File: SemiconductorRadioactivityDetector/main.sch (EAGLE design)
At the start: 41 parts, among them IC1 78L08Z, IC2 OPA2333D, IC3 OPA2333D, J1 22-05-7028-02, Q1 2N4093

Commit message: Third HW revision, paritialy done.
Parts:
- removed C10: 4p7, resistor:C-EUC0805
- removed C11: 10n, resistor:C-EUC0805
- removed C12: 10n, rcl:C-EUC0805
- removed C13: 100n, rcl:C-EUC0805
- removed C14, C15, C9: 100p, resistor:C-EUC0805
- removed C16: 100n, resistor:C-EUC0805
- removed IC3: OPA2333D, linear:OPA2333D
- removed J1: 22-05-7028-02, con-molex:22-05-7028-02
- removed PAD1, PAD2: (no value), wirepad:1,6/0,8
- removed Q1: 2N4093, transistor-fet:2N4093
- removed R11: 1k, rcl:R-EU_R0805
- removed R12, R13: 10k, rcl:R-EU_R0805
- removed TP1, TP2, TP5: PTR1TP12R, testpad:PTR1TP12R
- added D2, D3: BPW32, opto-trans-siemens:BPW32
- added SL1: (no value), con-amp-quick:M02
- added U1: TPS7A470, regulator-jqi:TPS7A470
- added X1: LTI-SASF54GT, con-coax:LTI-SASF54GT
- C1, C5: value 100n -> 330n
- C2: value 330n -> (none); device rcl:C-EUC0805 -> resistor:CPOL-EUT/3528-12R
- C3: value 100u/16V -> 100n; device rcl:CPOL-EU153CLV-0505 -> rcl:C-EUC0805
- C6: value 10n -> 100n; device resistor:C-EUC0805 -> rcl:C-EUC0805
- C7: value 10n -> 330n; device resistor:C-EUC0805 -> rcl:C-EUC0805
- C8: value 100n -> 330n; device rcl:C-EUC0805 -> rcl:C-EUC1206K
- D1: value BP104 -> BPW32; device opto-trans-siemens:BP104 -> opto-trans-siemens:BPW32
- IC1: value 78L08Z -> LF356D; device linear:78L08Z -> linear:LF356D
- IC2: value OPA2333D -> LF356D; device linear:OPA2333D -> linear:LF356D
- R1: value 10M -> 10k; device resistor:R-EU_0204/2V -> rcl:R-EU_R1206
- R10, R7: value 1k -> 10k
- R3: value 10k -> (none); device rcl:R-EU_R0805 -> resistor:R-EU_MELF0204W
- R4: value 470k -> (none); device rcl:R-EU_R0805 -> resistor:R-EU_MELF0204W
- R5: value 39k -> (none); device rcl:R-EU_R0805 -> resistor:R-TRIMM64W
- R6: value 10R -> (none); device rcl:R-EU_R0805 -> resistor:R-EU_M0805
- R8: value 10k -> (none); device rcl:R-EU_R0805 -> resistor:R-EU_M0805
- R9: value 10M -> (none); device rcl:R-EU_0204/2V -> resistor:R-EU_M0805
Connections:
- removed net N$11: C7.2, R7.2
- removed net N$13: C14.1, IC2B.-IN, R11.1, R12.2
- removed net N$16: C2.1, D1.C, R4.2
- removed net N$17: D1.A, Q1.G, R1.1
- removed net N$20: C10.2, C11.1, IC3A.OUT, R9.1
- removed net N$22: C12.1, C9.2, IC2A.OUT, R8.1
- removed net V_REF: C1.1, IC2A.+IN, IC2B.+IN, IC3A.+IN, IC3B.+IN, R2.1, R3.2, TP1.TP
- new net N$1: C5.2, C8.1, IC1.OUT, R4.2
- new net N$5: C6.1, U1.NR
- net GND: now also C2.-, C3.2, C6.2, C7.2, D1.A, D2.A, D3.A, IC1.V-, IC2.V-, R10.1, R2.1, R6.1, SL1.1, U1.0.1, U1.0.2, U1.0.4, U1.0.8, U1.1.6, U1.3.2, U1.6.4A, U1.6.4B, U1.GND, X1.2; no longer C13.2, C16.2, C2.2, C3.-, C5.2, C8.2, IC1.GND, IC2P.V-, IC3P.V-, J1-2.S, PAD2.P, Q1.S, R1.2, R3.1
- net N$10: now also C8.2, IC2.+IN, R10.2; no longer C9.1, IC2A.-IN, R8.2
- net N$14: now also C1.1, IC1.+IN, R1.1, R2.2; no longer C12.2, R11.2
- net N$15: now also R9.2, X1.1; no longer C11.2, R10.2
- net N$2: now also IC2.-IN, R8.1; no longer C6.2
- net N$3: now also R3.2, R4.1; no longer C14.2, IC2B.OUT, PAD1.P, R12.1
- net N$4: now also C5.1, D1.C, D2.C, D3.C, IC1.-IN, R3.1; no longer C10.1, IC3A.-IN, R6.1, R9.2
- net N$6: now also IC1.ON1, R5.A; no longer C6.1, Q1.D, R5.1
- net N$7: now also IC1.ON2, R5.E; no longer C15.2, C7.1, IC3B.OUT, R13.1, TP5.TP
- net N$8: now also C2.+, C3.1, SL1.2, U1.EN, U1.IN; no longer C3.+, C5.1, IC1.VI, J1-1.S, TP2.TP
- net N$9: now also IC2.OUT, R8.2, R9.1; no longer C15.1, IC3B.-IN, R10.1, R13.2
- net V+: now also C7.1, IC1.V+, IC2.V+, R1.2, R5.S, R7.2, U1.OUT, U1.SENSE; no longer C13.1, C16.1, C8.1, IC1.VO, IC2P.V+, IC3P.V+, R2.2, R4.1, R5.2
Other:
- moved on the sheet: C1, C4, C5, C6, C7, C8, D1, R1, R10, R2, R3, R4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

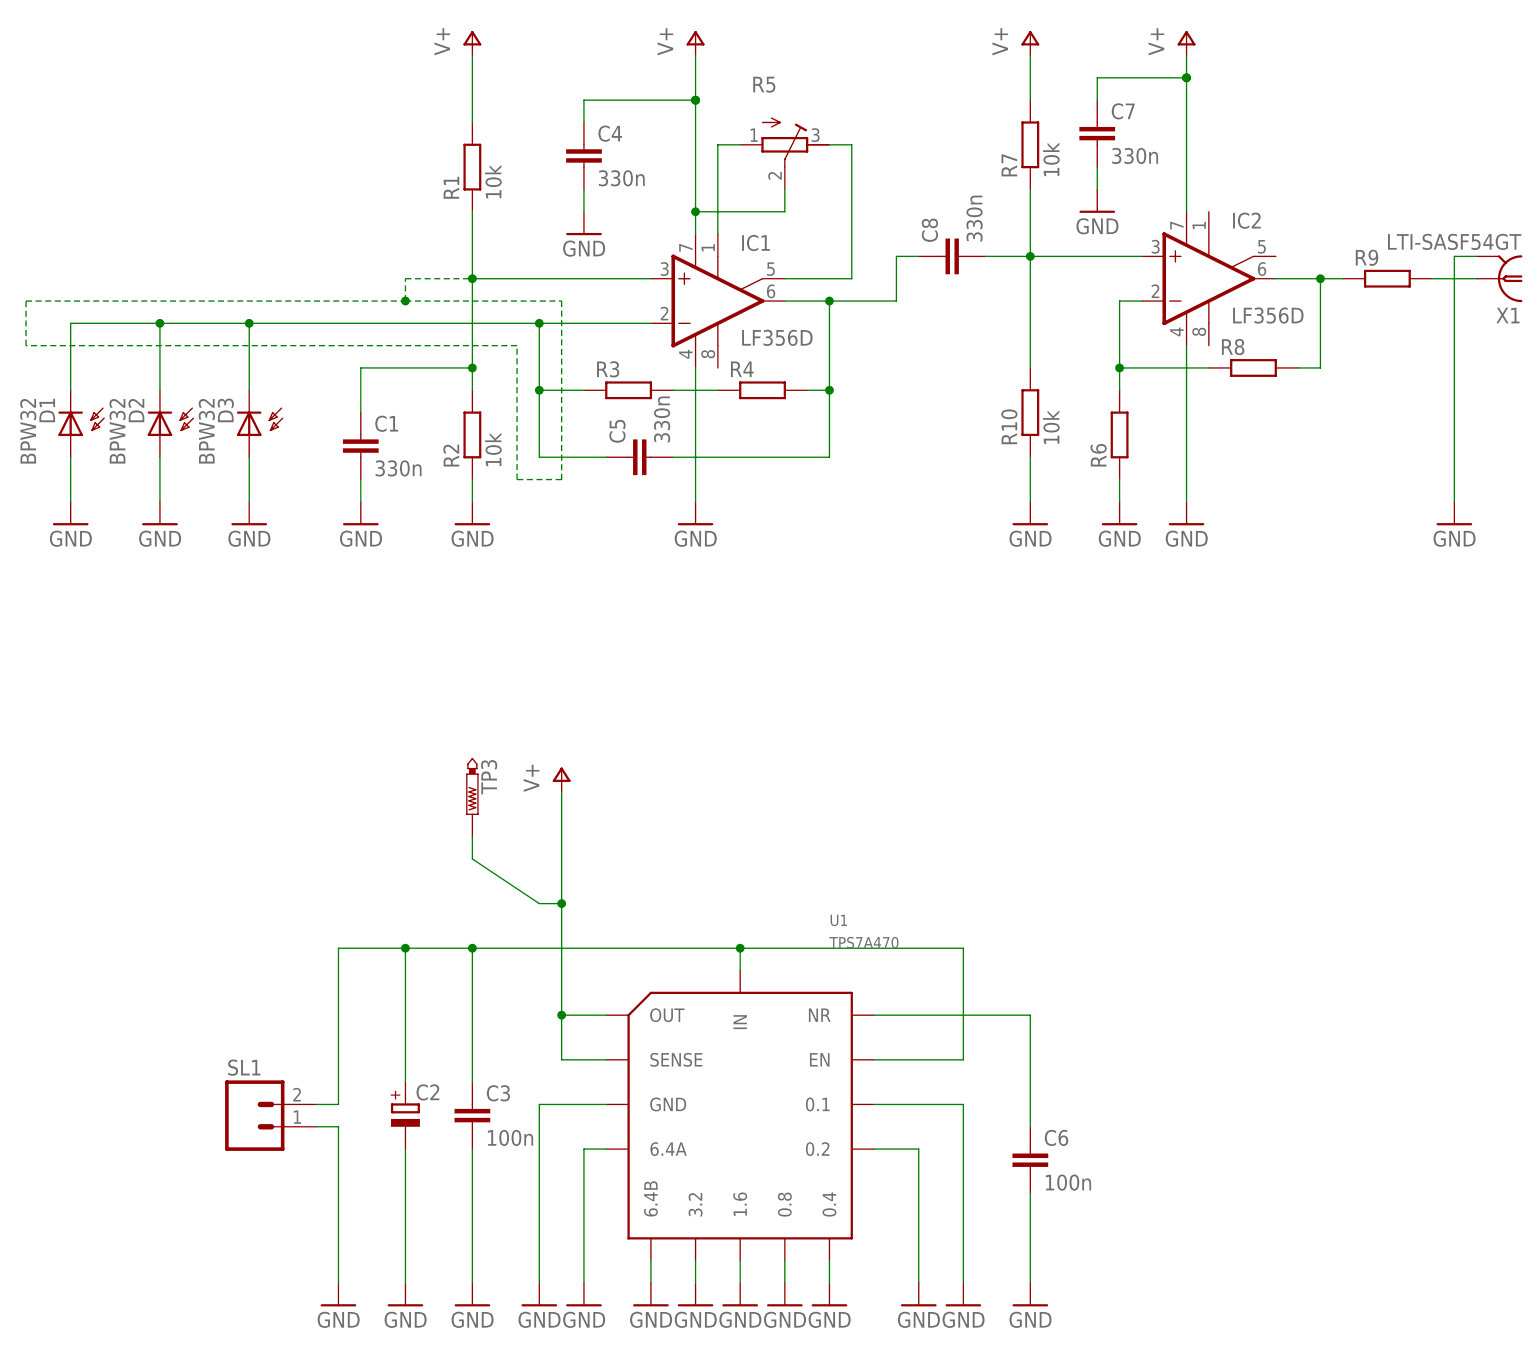
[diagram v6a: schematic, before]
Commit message: Removed obsolete project, PCB fixes.
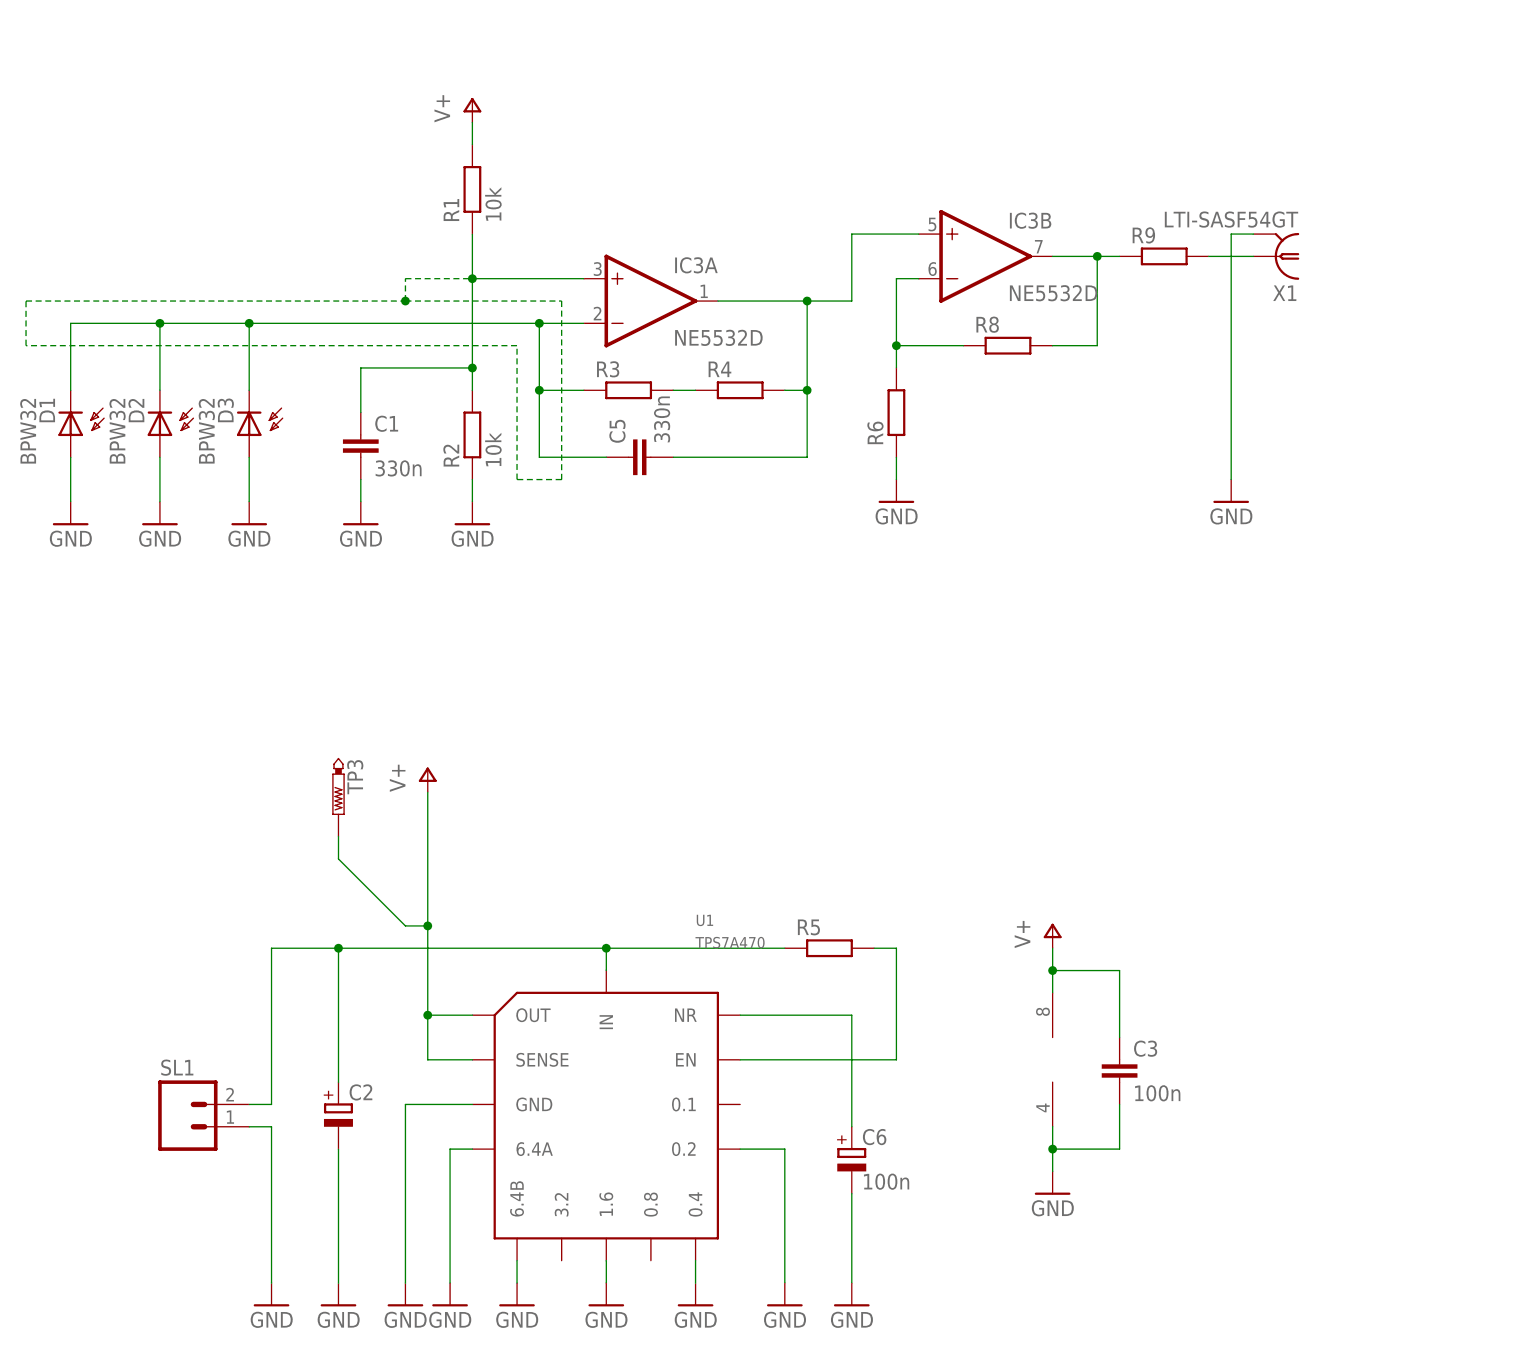
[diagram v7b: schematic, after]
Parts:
- removed C4, C7: 330n, rcl:C-EUC0805
- removed C8: 330n, rcl:C-EUC1206K
- removed IC1, IC2: LF356D, linear:LF356D
- removed R10, R7: 10k, rcl:R-EU_R0805
- added IC3: NE5532D, linear:NE5532D
- C6: device rcl:C-EUC0805 -> rcl:CPOL-EUA/3216-18W
- R1: device rcl:R-EU_R1206 -> rcl:R-EU_R0805
- R5: device resistor:R-TRIMM64W -> resistor:R-EU_M1206
- R6, R9: device resistor:R-EU_M0805 -> resistor:R-EU_0204/2V
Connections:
- removed net N$10: C8.2, IC2.+IN, R10.2, R7.1
- removed net N$7: IC1.ON2, R5.E
- net GND: now also C6.-, IC3P.V-; no longer C4.2, C6.2, C7.2, IC1.V-, IC2.V-, R10.1, U1.0.1, U1.0.8, U1.3.2
- net N$1: now also IC3A.OUT, IC3B.+IN; no longer C8.1, IC1.OUT
- net N$14: now also IC3A.+IN; no longer IC1.+IN
- net N$2: now also IC3B.-IN; no longer IC2.-IN
- net N$4: now also IC3A.-IN; no longer IC1.-IN
- net N$5: now also C6.+; no longer C6.1
- net N$6: now also R5.2, U1.EN; no longer IC1.ON1, R5.A
- net N$8: now also R5.1; no longer C3.1, U1.EN
- net N$9: now also IC3B.OUT; no longer IC2.OUT
- net V+: now also C3.1, IC3P.V+; no longer C4.1, C7.1, IC1.V+, IC2.V+, R5.S, R7.2
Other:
- moved on the sheet: C2, C3, R1, R4, R6, R8, R9, SL1, TP3, U1, X1
